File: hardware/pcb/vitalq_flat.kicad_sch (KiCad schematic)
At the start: 292 parts, among them J1 USB-C, J10 Optical tail pads, J11 Sweat site, J12 FH12-14S, J13 MX ECG pads, J2 LiPo pads, J3 FSR pads, J5 ECG pads, J6 EDA pads, J7 Chest bioZ, J8 TC2030, J9 I2C tail pads, Q1 CSD13380F3T, Q2 CSD13380F3T, Q3 BC847BS,115, Q4 CSD13380F3T, SW1 TS-1088, SW2 TS-1088, U1 ESP32-S3-MINI-1-N4R2, U10 AS7341-DLGM, U11 TMP117AIDRVR, U12 MLX90632SLD-DCB-100-SP, U13 BME280, U14 LSM6DSV80XTR, U15 TPS61240YFFR, U16 SFH 7072, U17 MAX17048G+T10, U18 W25Q512JVEIQ, U19 TCA6408ARSVR, U2 BQ25170DSGR, U20 TMP117AIDRVR, U21 USBLC6-2SC6, U22 MAX86178ENJ+, U23 SHT45-AD1B, U24 RV-3028-C7, U25 IM69D130, U3 TPS63802DLAR, U4 TPS7A2018PDBVR, U5 CP2102N-A02-GQFN28R, U6 AFE4900YZR, U7 AD5940BCBZ-RL7, U8 ADS1292RIRSMT, U9 PCA9306DCUR

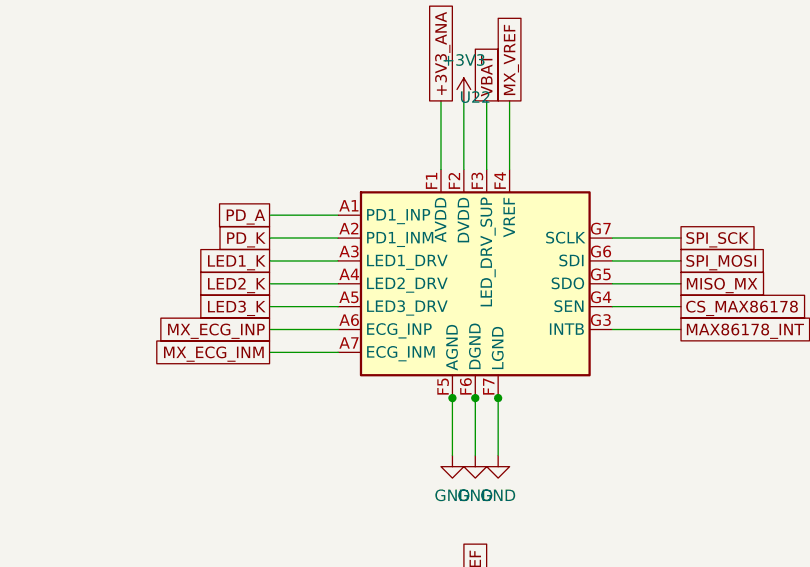
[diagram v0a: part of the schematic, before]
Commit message: U22 MAX86178: real 49-ball WLP footprint + pin map from ADI/Ultra Librarian model; remap nets by function
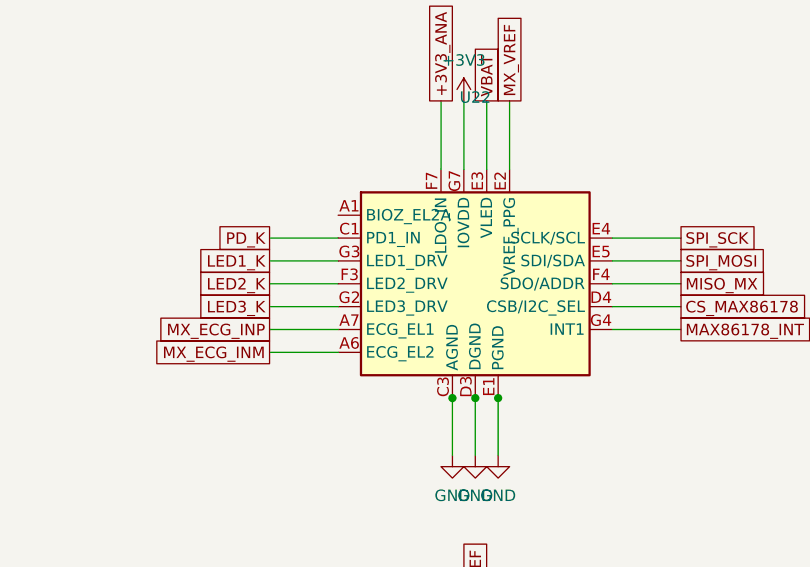
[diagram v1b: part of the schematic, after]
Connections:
- net +3V3: now also U22.G7 (IOVDD); no longer U22.F2 (DVDD)
- net +3V3_ANA: now also U22.F7 (LDO_IN); no longer U22.F1 (AVDD)
- net CS_MAX86178: now also U22.D4 (CSB/I2C_SEL); no longer U22.G4 (SEN)
- net GND: now also U22.C3 (AGND), U22.D3 (DGND), U22.E1 (PGND); no longer U22.F5 (AGND), U22.F6 (DGND), U22.F7 (LGND)
- net LED1_K: now also U22.G3 (LED1_DRV); no longer U22.A3 (LED1_DRV)
- net LED2_K: now also U22.F3 (LED2_DRV); no longer U22.A4 (LED2_DRV)
- net LED3_K: now also U22.G2 (LED3_DRV); no longer U22.A5 (LED3_DRV)
- net MAX86178_INT: now also U22.G4 (INT1); no longer U22.G3 (INTB)
- net MISO_MX: now also U22.F4 (SDO/ADDR); no longer U22.G5 (SDO)
- net MX_ECG_INM: now also U22.A6 (ECG_EL2); no longer U22.A7 (ECG_INM)
- net MX_ECG_INP: now also U22.A7 (ECG_EL1); no longer U22.A6 (ECG_INP)
- net MX_VREF: now also U22.E2 (VREF_PPG); no longer U22.F4 (VREF)
- net PD_A: no longer U22.A1 (PD1_INP)
- net PD_K: now also U22.C1 (PD1_IN); no longer U22.A2 (PD1_INM)
- net SPI_MOSI: now also U22.E5 (SDI/SDA); no longer U22.G6 (SDI)
- net SPI_SCK: now also U22.E4 (SCLK/SCL); no longer U22.G7 (SCLK)
- net VBAT: now also U22.E3 (VLED); no longer U22.F3 (LED_DRV_SUP)
- net AVDD: now reaches U22.D6 (AVDD)
- net DVDD: now reaches U22.D7 (DVDD)
- net LDO_OUT: now reaches U22.E7 (LDO_OUT)
